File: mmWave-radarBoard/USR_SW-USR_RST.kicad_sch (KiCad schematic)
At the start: 22 parts, among them SW501 SW_DPST, SW502 SW_DPST, U501 SN74LVC1G11DSFR

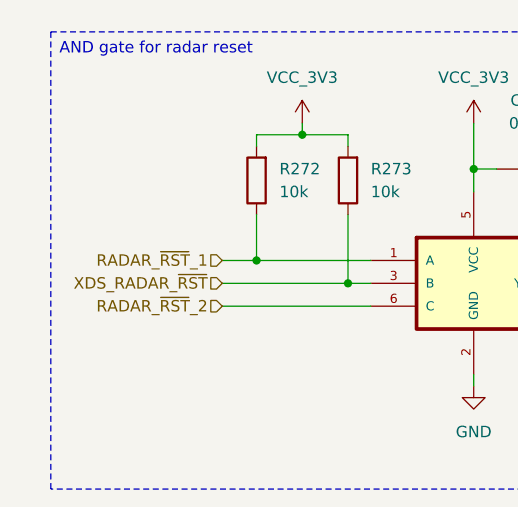
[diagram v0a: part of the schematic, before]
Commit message: Updated schematic of the radar module
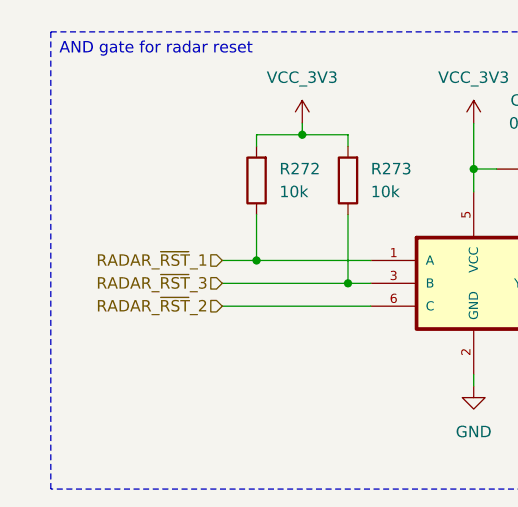
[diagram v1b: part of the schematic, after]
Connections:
- net XDS_RADAR_~{RST} renamed RADAR_~{RST}_3
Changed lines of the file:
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@@
 		)
 	)
-	(hierarchical_label "XDS_RADAR_~{RST}"
+	(hierarchical_label "RADAR_~{RST}_3"
 		(shape input)
 		(at 64.77 128.27 180)

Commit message: Removed unnecessary bits
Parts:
- removed C286, C287: 0.1uF, symbol Device:C
- removed D501: LED RED, symbol Device:LED
- removed D502, D503: LED GREEN, symbol Device:LED
- removed MOSFET501, MOSFET502: SSM3K35AMFV_L3F, symbol SSM3K35AMFV:SSM3K35AMFV_L3F
- removed R272, R273: 10k, symbol Device:R
- removed R274, R279: 0, symbol Device:R
- removed R275, R276, R277: 100k, symbol Device:R
- removed R278, R282: 2.2k, symbol Device:R
- removed R280: 4.7k, symbol Device:R
- removed R281, R283: 510, symbol Device:R
- removed SW501, SW502: SW_DPST, symbol Switch:SW_DPST
- removed U501: SN74LVC1G11DSFR, SN74LVC1G11DSFR:SON35P100X100X40-6N, symbol SN74LVC1G11DSFR:SN74LVC1G11DSFR
